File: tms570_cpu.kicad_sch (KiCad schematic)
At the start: 51 parts, among them J12 TS-103-G-A, J2 FTSH-105-01-L-DV-K, U2 TMS570LS0914PGE

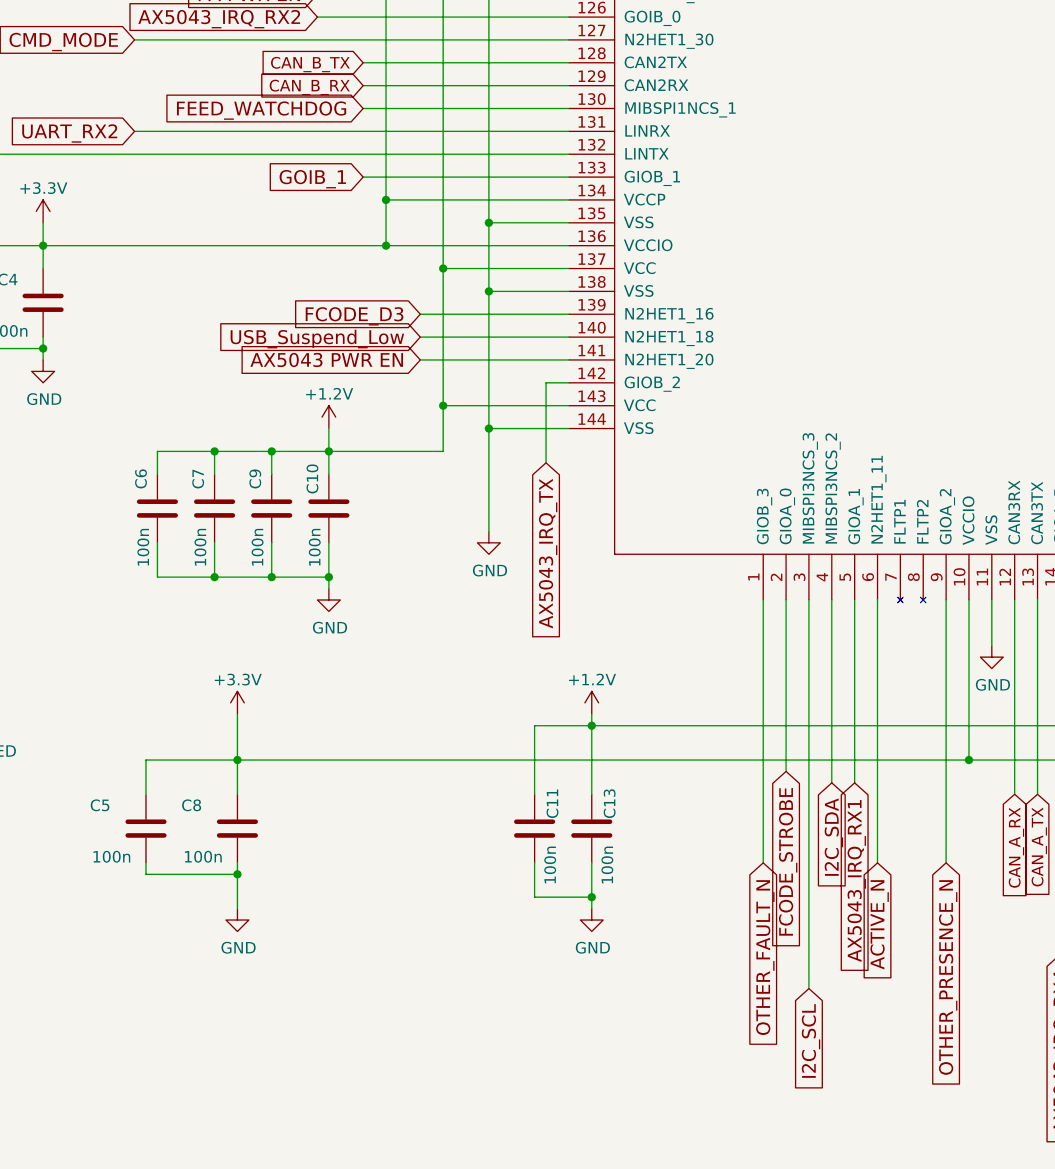
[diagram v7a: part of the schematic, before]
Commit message: Moved ACTIVE\_N to a normal GPIO so it can be interrupt driven
Signed-off-by: Corey Minyard <corey@minyard.net>
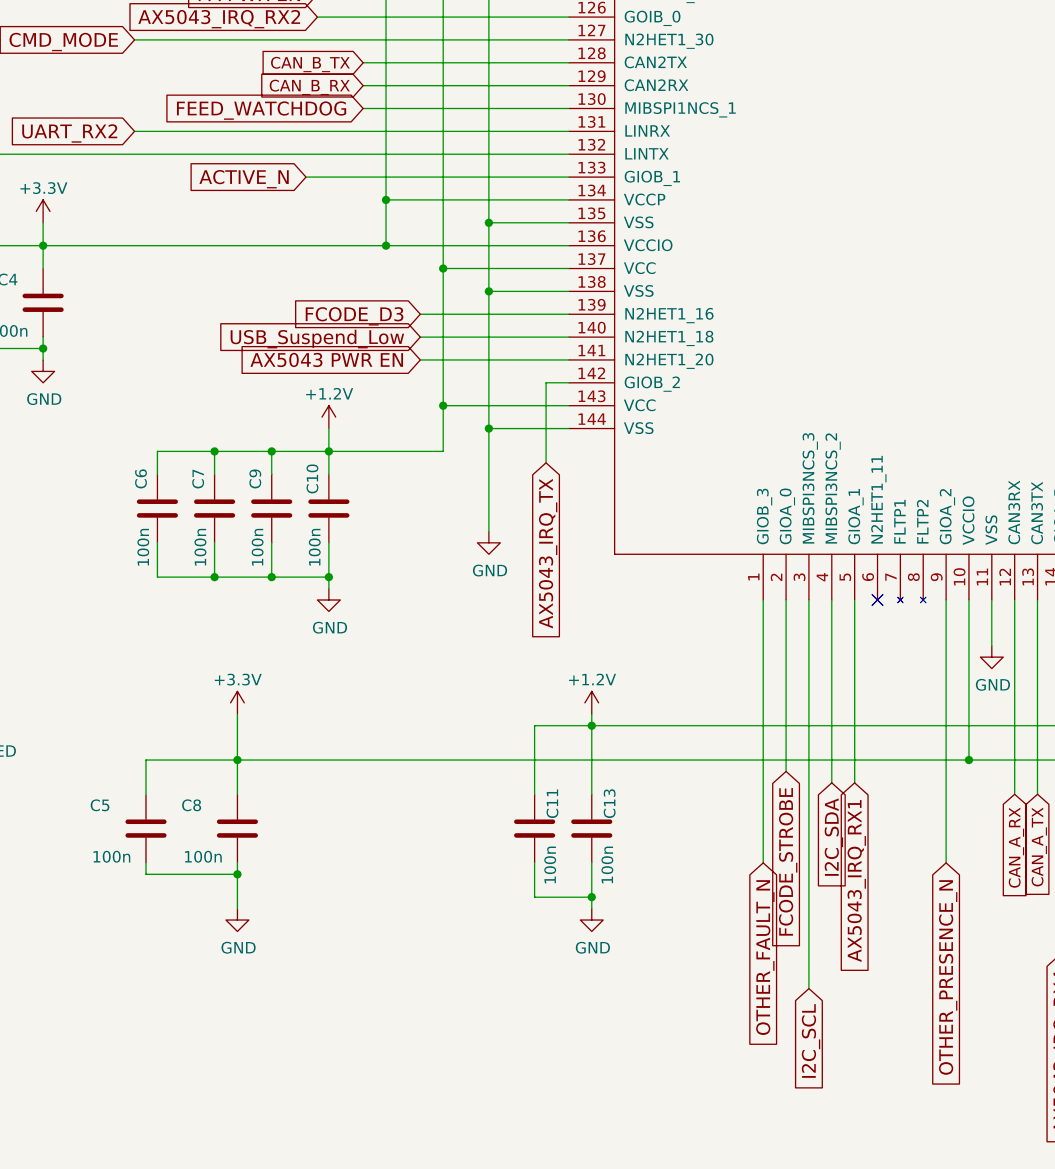
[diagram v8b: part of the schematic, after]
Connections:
- net GOIB_1 is gone; now on net ACTIVE_N: U2.133 (GIOB_1)
- net ACTIVE_N: no longer U2.6 (N2HET1_11)
- no-connect marks 16 -> 17
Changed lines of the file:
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@@
 	)
 	(no_connect
+		(at 184.15 204.47)
+	)
+	(no_connect
 		(at 227.33 72.39)
 	)
@@
 	(wire
 		(pts
-			(xy 184.15 204.47) (xy 184.15 233.68)
-		)
-		(stroke
-			(width 0)
-			(type default)
-		)
-	)
-	(wire
-		(pts
 			(xy 99.06 111.76) (xy 99.06 116.84)
 		)
@@
 	(wire
 		(pts
-			(xy 127 157.48) (xy 149.86 157.48)
-		)
-		(stroke
-			(width 0)
-			(type default)
-		)
-	)
-	(wire
-		(pts
 			(xy 309.88 59.69) (xy 313.69 59.69)
 		)
@@
 	(wire
 		(pts
+			(xy 149.86 157.48) (xy 120.65 157.48)
+		)
+		(stroke
+			(width 0)
+			(type default)
+		)
+	)
+	(wire
+		(pts
 			(xy 105.41 64.77) (xy 97.79 64.77)
 		)
@@
 		)
 	)
-	(global_label "ACTIVE_N"
-		(shape input)
-		(at 184.15 233.68 270)
-		(fields_autoplaced yes)
-		(effects
-			(font
-				(size 1.524 1.524)
-			)
-			(justify right)
-		)
-		(property "Intersheetrefs" "${INTERSHEET_REFS}"
-			(at 184.15 246.6368 90)
-			(effects
-				(font
-					(size 1.27 1.27)
-				)
-				(justify right)
-				(hide yes)
-			)
-		)
-	)
 	(global_label "MRAM_MISO"
 		(shape input)
@@
 		)
 	)
-	(global_label "GOIB_1"
-		(shape input)
-		(at 127 157.48 180)
-		(fields_autoplaced yes)
-		(effects
-			(font
-				(size 1.524 1.524)
-			)
-			(justify right)
-		)
-		(property "Intersheetrefs" "${INTERSHEET_REFS}"
-			(at 116.3158 157.48 0)
-			(effects
-				(font
-					(size 1.27 1.27)
-				)
-				(justify right)
-				(hide yes)
-			)
-		)
-	)
 	(global_label "PWR_FLAG_SSPA"
 		(shape input)
@@
 				(hide yes)
 			)
+		)
+	)
+	(global_label "ACTIVE_N"
+		(shape input)
+		(at 120.65 157.48 180)
+		(fields_autoplaced yes)
+		(effects
+			(font
+				(size 1.524 1.524)
+			)
+			(justify right)
+		)
+		(property "Intersheetrefs" "${INTERSHEET_REFS}"
+			(at 107.6932 157.48 0)
+			(effects
+				(font
+					(size 1.27 1.27)
+				)
+				(justify right)
+				(hide yes)
+			)
